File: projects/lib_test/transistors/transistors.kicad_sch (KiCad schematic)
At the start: 4 parts, among them Q1001 MMBT2222A, Q1002 AO3400A, Q1003 DMP3028LFDE, Q1004 CEM3083

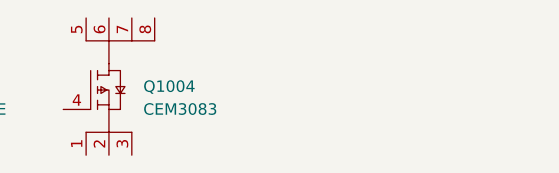
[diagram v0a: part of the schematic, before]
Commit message: add MOSFET N channel in SOIC8
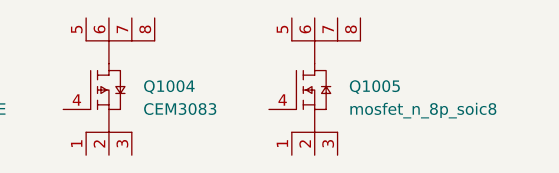
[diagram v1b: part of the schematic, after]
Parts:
- added Q1005: mosfet_n_8p_soic8, lily_footprints:soic8, symbol lily_symbols:mosfet_n_VBZA4800_soic8
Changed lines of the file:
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@@
+	)
+	(symbol
+		(lib_id "lily_symbols:mosfet_n_VBZA4800_soic8")
+		(at 121.92 27.94 0)
+		(unit 1)
+		(exclude_from_sim no)
+		(in_bom yes)
+		(on_board yes)
+		(dnp no)
+		(property "Reference" "Q1005"
+			(at 130.81 25.4 0)
+			(effects
+				(font
+					(size 1.27 1.27)
+				)
+				(justify left)
+			)
+		)
+		(property "Value" "mosfet_n_8p_soic8"
+			(at 130.81 27.94 0)
+			(effects
+				(font
+					(size 1.27 1.27)
+				)
+				(justify left)
+			)
+		)
+		(property "Footprint" "lily_footprints:soic8"
+			(at 127 45.72 0)
+			(effects
+				(font
+					(size 1.27 1.27)
+				)
+				(hide yes)
+			)
+		)
+		(property "Datasheet" ""
+			(at 116.84 30.48 0)
+			(effects
+				(font
+					(size 1.27 1.27)
+				)
+				(hide yes)
+			)
+		)
+		(property "Description" ""
+			(at 119.38 27.94 0)
+			(effects
+				(font
+					(size 1.27 1.27)
+				)
+				(hide yes)
+			)
+		)
+		(property "Revision" "1"
+			(at 127 40.64 0)
+			(effects
+				(font
+					(size 1.27 1.27)
+				)
+				(hide yes)
+			)
+		)
+		(property "Status" "Active"
+			(at 127 43.18 0)
+			(effects
+				(font
+					(size 1.27 1.27)
+				)
+				(hide yes)
+			)
+		)
+		(property "Manufacturer" "VBsemi"
+			(at 127 48.26 0)
+			(effects
+				(font
+					(size 1.27 1.27)
+				)
+				(hide yes)
+			)
+		)
+		(property "Manufacturer_ID" "VBZA4800"
+			(at 127 50.8 0)
+			(effects
+				(font
+					(size 1.27 1.27)
+				)
+				(hide yes)
+			)
+		)
+		(property "Lily_ID" "xxxx-yyyyy"
+			(at 127 53.34 0)
+			(effects
+				(font
+					(size 1.27 1.27)
+				)
+				(hide yes)
+			)
+		)
+		(property "JLCPCB_ID" "C700593"
+			(at 127 55.88 0)
+			(effects
+				(font
+					(size 1.27 1.27)
+				)
+				(hide yes)
+			)
+		)
+		(property "JLCPCB_STATUS" "Extended"
+			(at 127 58.42 0)
+			(effects
+				(font
+					(size 1.27 1.27)
+				)
+				(hide yes)
+			)
+		)
+		(pin "1"
+		)
+		(pin "4"
+		)
+		(pin "5"
+		)
+		(pin "6"
+		)
+		(pin "2"
+		)
+		(pin "7"
+		)
+		(pin "8"
+		)
+		(pin "3"
+		)
+		(instances
+			(project ""
+				(path "/e63e39d7-6ac0-4ffd-8aa3-1841a4541b55"
+					(reference "Q1005")
+					(unit 1)
+				)
+			)
+		)
 	)
 	(symbol

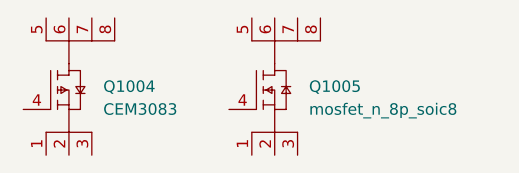
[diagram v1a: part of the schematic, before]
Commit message: updated value of N channel MOSFET
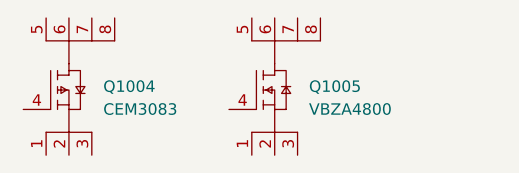
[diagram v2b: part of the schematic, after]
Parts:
- Q1005: value mosfet_n_8p_soic8 -> VBZA4800
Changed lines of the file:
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@@
 			)
 		)
-		(property "Value" "mosfet_n_8p_soic8"
+		(property "Value" "VBZA4800"
 			(at 130.81 27.94 0)
 			(effects

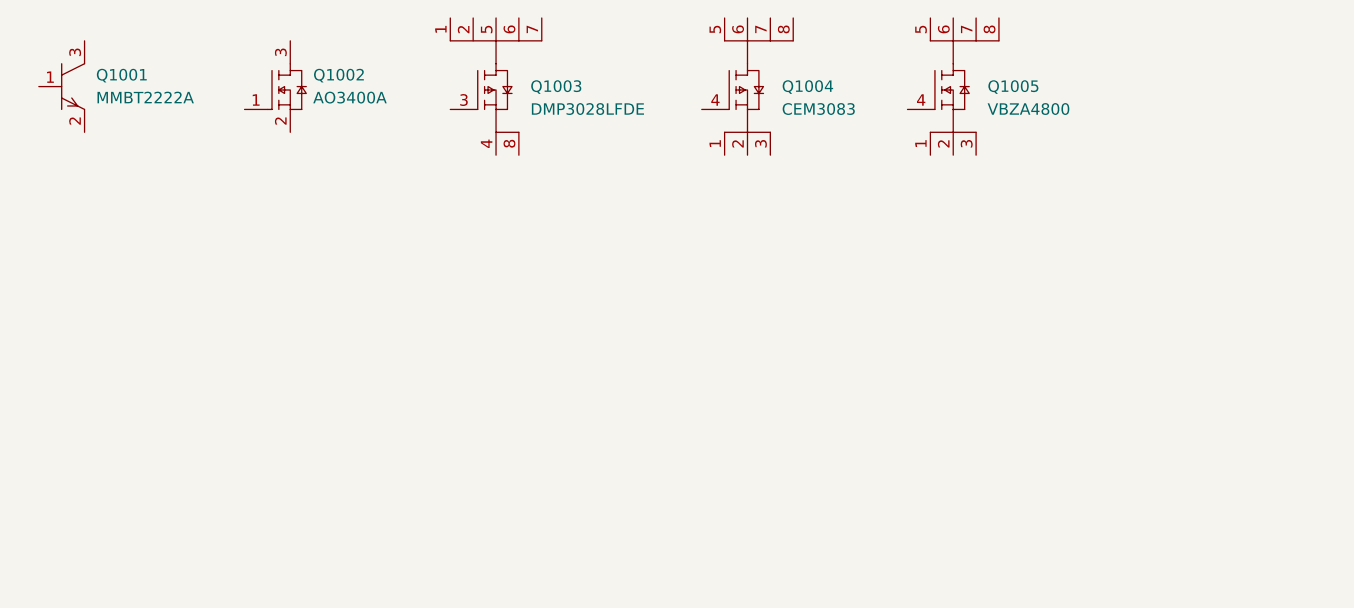
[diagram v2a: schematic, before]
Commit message: add transistors to the test design
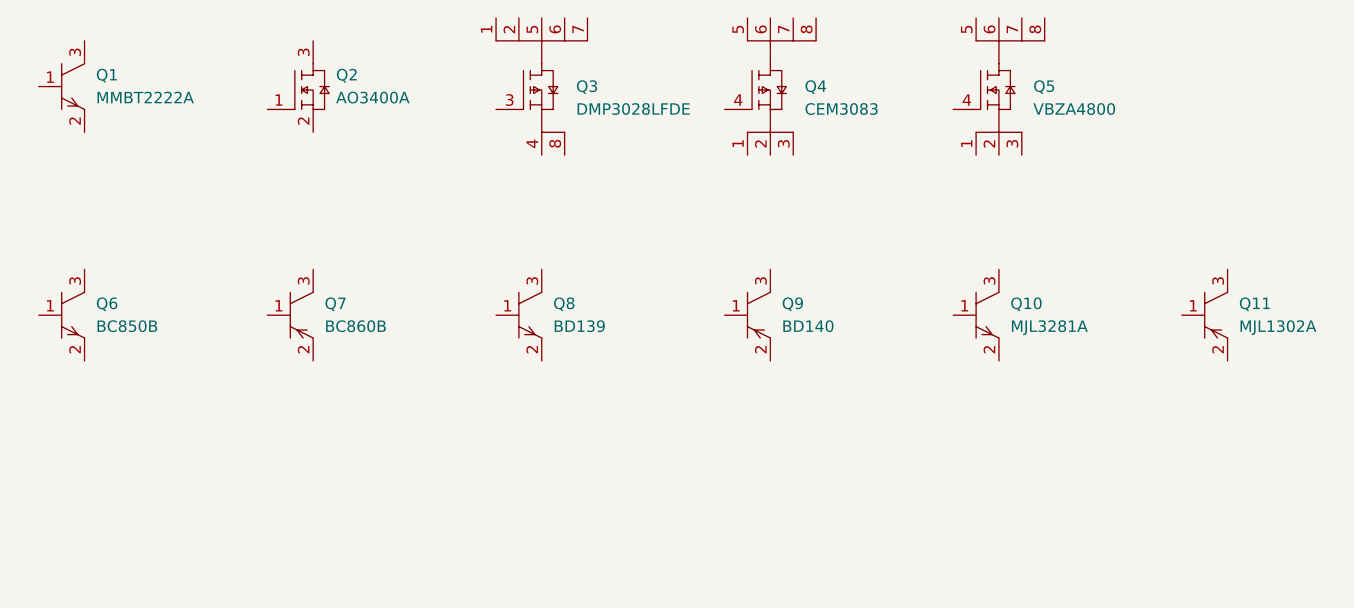
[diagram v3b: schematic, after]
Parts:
- added Q10: MJL3281A, lily_footprints:to264, symbol lily_symbols:bjt_npn_MJL3281A_to264
- added Q11: MJL1302A, lily_footprints:to264, symbol lily_symbols:bjt_pnp_MJL1302A_to264
- added Q6: BC850B, lily_footprints:sot23, symbol lily_symbols:bjt_npn_BC850B_sot23
- added Q7: BC860B, lily_footprints:sot23, symbol lily_symbols:bjt_pnp_BC860B_sot23
- added Q8: BD139, lily_footprints:to126, symbol lily_symbols:bjt_npn_BD139_to126
- added Q9: BD140, lily_footprints:to126, symbol lily_symbols:bjt_pnp_BD140_to126
- renumbered Q1001 to Q1, Q1002 to Q2, Q1003 to Q3, Q1004 to Q4, Q1005 to Q5
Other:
- moved on the sheet: Q2, Q3, Q4, Q5

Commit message: updated lib test
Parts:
- removed Q1: MMBT2222A, lily_footprints:sot23, symbol lily_symbols:bjt_npn_MMBT2222A_sot23
- removed Q2: AO3400A, lily_footprints:sot23, symbol lily_symbols:mosfet_n_AO3400A_sot23
- removed Q5: VBZA4800, lily_footprints:soic8, symbol lily_symbols:mosfet_n_VBZA4800_soic8
- added Q1007: MMBT2222AL, lily_footprints:sot23, symbol lily_symbols:bjt_npn_MMBT2222AL_sot23
- added Q1008: DMG3406L, lily_footprints:sot23, symbol lily_symbols:mosfet_n_DMG3406L_sot23
- Q1009: renamed from Q3; JLCPCB_STATUS Extended -> (none); Lily_ID 1918-10002 -> NO_ID; Manufacturer_ID DMP3028LFDE -> DMP3028LFDE-13
- renumbered Q6 to Q1001, Q7 to Q1002, Q8 to Q1003, Q9 to Q1004, Q10 to Q1005, Q11 to Q1006, Q4 to Q1010
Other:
- moved on the sheet: Q1001, Q1002, Q1003, Q1004, Q1005, Q1006, Q1009, Q1010

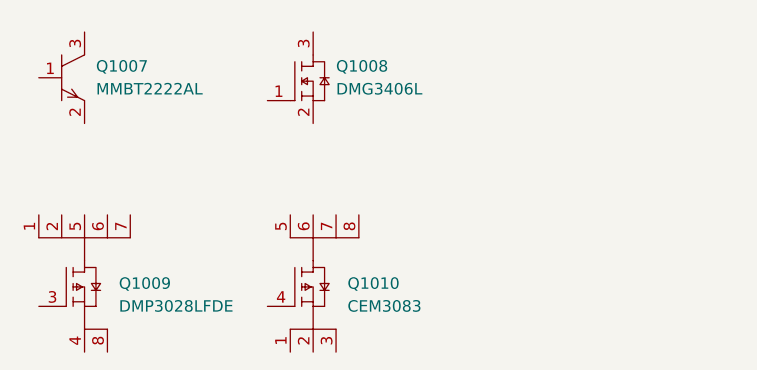
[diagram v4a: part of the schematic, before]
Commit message: removed unused test design stuff
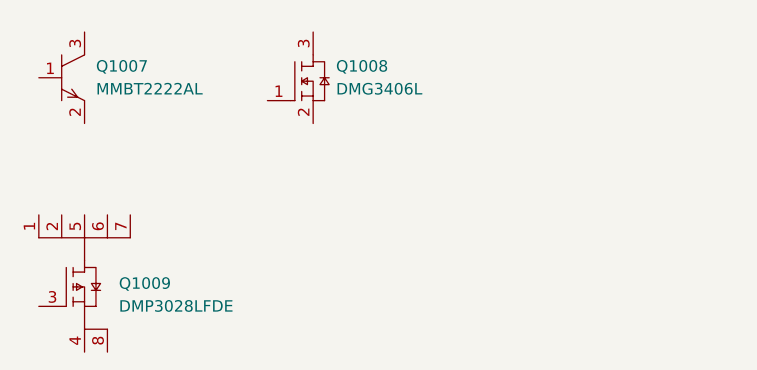
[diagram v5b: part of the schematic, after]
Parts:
- removed Q1010: CEM3083, lily_footprints:soic8, symbol lily_symbols:mosfet_p_CEM3083_soic8
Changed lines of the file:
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@@
-		)
-	)
-	(symbol
-		(lib_id "lily_symbols:mosfet_p_CEM3083_soic8")
-		(at 50.8 76.2 0)
-		(unit 1)
-		(exclude_from_sim no)
-		(in_bom yes)
-		(on_board yes)
-		(dnp no)
-		(property "Reference" "Q1010"
-			(at 59.69 73.66 0)
-			(effects
-				(font
-					(size 1.27 1.27)
-				)
-				(justify left)
-			)
-		)
-		(property "Value" "CEM3083"
-			(at 59.69 76.2 0)
-			(effects
-				(font
-					(size 1.27 1.27)
-				)
-				(justify left)
-			)
-		)
-		(property "Footprint" "lily_footprints:soic8"
-			(at 55.88 93.98 0)
-			(effects
-				(font
-					(size 1.27 1.27)
-				)
-				(hide yes)
-			)
-		)
-		(property "Datasheet" ""
-			(at 45.72 78.74 0)
-			(effects
-				(font
-					(size 1.27 1.27)
-				)
-				(hide yes)
-			)
-		)
-		(property "Description" ""
-			(at 48.26 76.2 0)
-			(effects
-				(font
-					(size 1.27 1.27)
-				)
-				(hide yes)
-			)
-		)
-		(property "Revision" "1"
-			(at 55.88 88.9 0)
-			(effects
-				(font
-					(size 1.27 1.27)
-				)
-				(hide yes)
-			)
-		)
-		(property "Status" "Active"
-			(at 55.88 91.44 0)
-			(effects
-				(font
-					(size 1.27 1.27)
-				)
-				(hide yes)
-			)
-		)
-		(property "Manufacturer" "CET"
-			(at 55.88 96.52 0)
-			(effects
-				(font
-					(size 1.27 1.27)
-				)
-				(hide yes)
-			)
-		)
-		(property "Manufacturer_ID" "CEM3083"
-			(at 55.88 99.06 0)
-			(effects
-				(font
-					(size 1.27 1.27)
-				)
-				(hide yes)
-			)
-		)
-		(property "Lily_ID" "xxxx-yyyyy"
-			(at 55.88 101.6 0)
-			(effects
-				(font
-					(size 1.27 1.27)
-				)
-				(hide yes)
-			)
-		)
-		(property "JLCPCB_ID" "C83039"
-			(at 55.88 104.14 0)
-			(effects
-				(font
-					(size 1.27 1.27)
-				)
-				(hide yes)
-			)
-		)
-		(property "JLCPCB_STATUS" "Extended"
-			(at 55.88 106.68 0)
-			(effects
-				(font
-					(size 1.27 1.27)
-				)
-				(hide yes)
-			)
-		)
-		(pin "5"
-		)
-		(pin "4"
-		)
-		(pin "6"
-		)
-		(pin "1"
-		)
-		(pin "2"
-		)
-		(pin "7"
-		)
-		(pin "3"
-		)
-		(pin "8"
-		)
-		(instances
-			(project ""
-				(path "/e63e39d7-6ac0-4ffd-8aa3-1841a4541b55"
-					(reference "Q1010")
-					(unit 1)
-				)
-			)
 		)
 	)
